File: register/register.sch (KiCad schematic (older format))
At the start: 38 parts, among them U1 74LS244, U2 74LS244, U3 74LS377, U4 74LS377

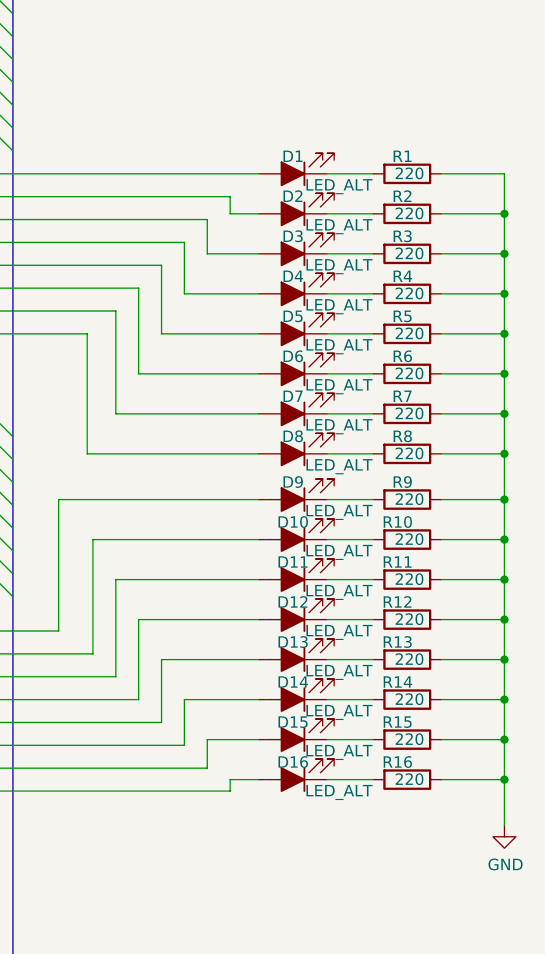
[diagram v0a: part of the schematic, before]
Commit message: route alu, upde register
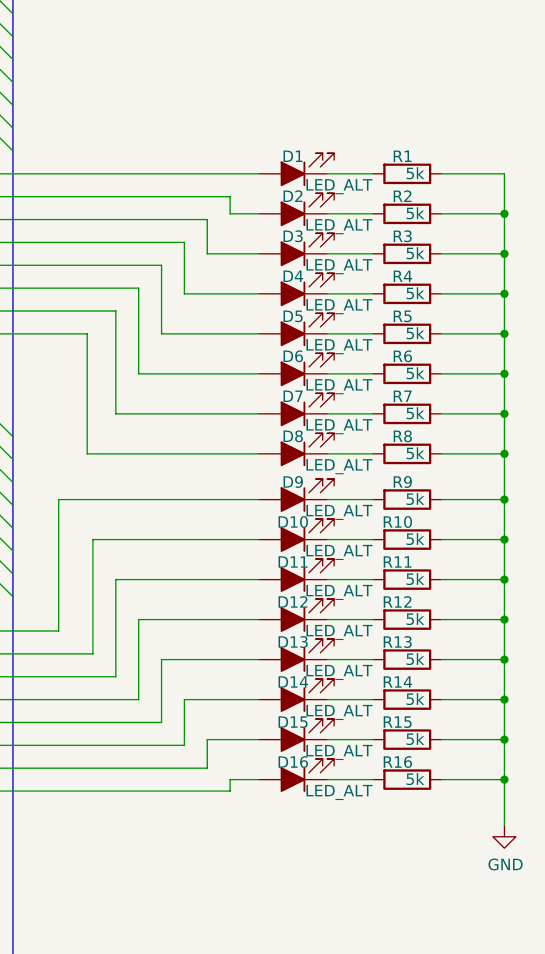
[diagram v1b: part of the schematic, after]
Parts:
- R1, R10, R11, R12, R13, R14, R15, R16, R2, R3, R4, R5, R6, R7, R8, R9: value 220 -> 5k
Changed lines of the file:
@@
 AR Path="/5EBAD929/5EC056B8" Ref="R2"  Part="1"
 F 0 "R2" V 10050 2475 50  0000 R CNN
-F 1 "220" V 10125 2525 50  0000 R CNN
+F 1 "5k" V 10125 2525 50  0000 R CNN
 F 2 "Resistor_THT:R_Axial_DIN0207_L6.3mm_D2.5mm_P7.62mm_Horizontal" V 10055 2450 50  0001 C CNN
 F 3 "~" H 10125 2450 50  0001 C CNN
@@
 AR Path="/5EBAD929/5EC056BE" Ref="R3"  Part="1"
 F 0 "R3" V 10050 2650 50  0000 R CNN
-F 1 "220" V 10125 2700 50  0000 R CNN
+F 1 "5k" V 10125 2700 50  0000 R CNN
 F 2 "Resistor_THT:R_Axial_DIN0207_L6.3mm_D2.5mm_P7.62mm_Horizontal" V 10055 2625 50  0001 C CNN
 F 3 "~" H 10125 2625 50  0001 C CNN
@@
 AR Path="/5EBAD929/5EC056C4" Ref="R4"  Part="1"
 F 0 "R4" V 10050 2825 50  0000 R CNN
-F 1 "220" V 10125 2875 50  0000 R CNN
+F 1 "5k" V 10125 2875 50  0000 R CNN
 F 2 "Resistor_THT:R_Axial_DIN0207_L6.3mm_D2.5mm_P7.62mm_Horizontal" V 10055 2800 50  0001 C CNN
 F 3 "~" H 10125 2800 50  0001 C CNN
@@
 AR Path="/5EBAD929/5EC056CA" Ref="R5"  Part="1"
 F 0 "R5" V 10050 3000 50  0000 R CNN
-F 1 "220" V 10125 3050 50  0000 R CNN
+F 1 "5k" V 10125 3050 50  0000 R CNN
 F 2 "Resistor_THT:R_Axial_DIN0207_L6.3mm_D2.5mm_P7.62mm_Horizontal" V 10055 2975 50  0001 C CNN
 F 3 "~" H 10125 2975 50  0001 C CNN
@@
 AR Path="/5EBAD929/5EC056D0" Ref="R6"  Part="1"
 F 0 "R6" V 10050 3175 50  0000 R CNN
-F 1 "220" V 10125 3225 50  0000 R CNN
+F 1 "5k" V 10125 3225 50  0000 R CNN
 F 2 "Resistor_THT:R_Axial_DIN0207_L6.3mm_D2.5mm_P7.62mm_Horizontal" V 10055 3150 50  0001 C CNN
 F 3 "~" H 10125 3150 50  0001 C CNN
@@
 AR Path="/5EBAD929/5EC056D6" Ref="R7"  Part="1"
 F 0 "R7" V 10050 3350 50  0000 R CNN
-F 1 "220" V 10125 3400 50  0000 R CNN
+F 1 "5k" V 10125 3400 50  0000 R CNN
 F 2 "Resistor_THT:R_Axial_DIN0207_L6.3mm_D2.5mm_P7.62mm_Horizontal" V 10055 3325 50  0001 C CNN
 F 3 "~" H 10125 3325 50  0001 C CNN
@@
 AR Path="/5EBAD929/5EC056DC" Ref="R8"  Part="1"
 F 0 "R8" V 10050 3525 50  0000 R CNN
-F 1 "220" V 10125 3575 50  0000 R CNN
+F 1 "5k" V 10125 3575 50  0000 R CNN
 F 2 "Resistor_THT:R_Axial_DIN0207_L6.3mm_D2.5mm_P7.62mm_Horizontal" V 10055 3500 50  0001 C CNN
 F 3 "~" H 10125 3500 50  0001 C CNN
@@
 AR Path="/5EBAD929/5EC056E2" Ref="R9"  Part="1"
 F 0 "R9" V 10050 3725 50  0000 R CNN
-F 1 "220" V 10125 3775 50  0000 R CNN
+F 1 "5k" V 10125 3775 50  0000 R CNN
 F 2 "Resistor_THT:R_Axial_DIN0207_L6.3mm_D2.5mm_P7.62mm_Horizontal" V 10055 3700 50  0001 C CNN
 F 3 "~" H 10125 3700 50  0001 C CNN
@@
 AR Path="/5EBAD929/5EC056E8" Ref="R10"  Part="1"
 F 0 "R10" V 10050 3900 50  0000 R CNN
-F 1 "220" V 10125 3950 50  0000 R CNN
+F 1 "5k" V 10125 3950 50  0000 R CNN
 F 2 "Resistor_THT:R_Axial_DIN0207_L6.3mm_D2.5mm_P7.62mm_Horizontal" V 10055 3875 50  0001 C CNN
 F 3 "~" H 10125 3875 50  0001 C CNN
@@
 AR Path="/5EBAD929/5EC056EE" Ref="R11"  Part="1"
 F 0 "R11" V 10050 4075 50  0000 R CNN
-F 1 "220" V 10125 4125 50  0000 R CNN
+F 1 "5k" V 10125 4125 50  0000 R CNN
 F 2 "Resistor_THT:R_Axial_DIN0207_L6.3mm_D2.5mm_P7.62mm_Horizontal" V 10055 4050 50  0001 C CNN
 F 3 "~" H 10125 4050 50  0001 C CNN
@@
 AR Path="/5EBAD929/5EC056F4" Ref="R12"  Part="1"
 F 0 "R12" V 10050 4250 50  0000 R CNN
-F 1 "220" V 10125 4300 50  0000 R CNN
+F 1 "5k" V 10125 4300 50  0000 R CNN
 F 2 "Resistor_THT:R_Axial_DIN0207_L6.3mm_D2.5mm_P7.62mm_Horizontal" V 10055 4225 50  0001 C CNN
 F 3 "~" H 10125 4225 50  0001 C CNN
@@
 AR Path="/5EBAD929/5EC056FA" Ref="R13"  Part="1"
 F 0 "R13" V 10050 4425 50  0000 R CNN
-F 1 "220" V 10125 4475 50  0000 R CNN
+F 1 "5k" V 10125 4475 50  0000 R CNN
 F 2 "Resistor_THT:R_Axial_DIN0207_L6.3mm_D2.5mm_P7.62mm_Horizontal" V 10055 4400 50  0001 C CNN
 F 3 "~" H 10125 4400 50  0001 C CNN
@@
 AR Path="/5EBAD929/5EC05700" Ref="R14"  Part="1"
 F 0 "R14" V 10050 4600 50  0000 R CNN
-F 1 "220" V 10125 4650 50  0000 R CNN
+F 1 "5k" V 10125 4650 50  0000 R CNN
 F 2 "Resistor_THT:R_Axial_DIN0207_L6.3mm_D2.5mm_P7.62mm_Horizontal" V 10055 4575 50  0001 C CNN
 F 3 "~" H 10125 4575 50  0001 C CNN
@@
 AR Path="/5EBAD929/5EC05706" Ref="R15"  Part="1"
 F 0 "R15" V 10050 4775 50  0000 R CNN
-F 1 "220" V 10125 4825 50  0000 R CNN
+F 1 "5k" V 10125 4825 50  0000 R CNN
 F 2 "Resistor_THT:R_Axial_DIN0207_L6.3mm_D2.5mm_P7.62mm_Horizontal" V 10055 4750 50  0001 C CNN
 F 3 "~" H 10125 4750 50  0001 C CNN
@@
 AR Path="/5EBAD929/5EC0570C" Ref="R16"  Part="1"
 F 0 "R16" V 10050 4950 50  0000 R CNN
-F 1 "220" V 10125 5000 50  0000 R CNN
+F 1 "5k" V 10125 5000 50  0000 R CNN
 F 2 "Resistor_THT:R_Axial_DIN0207_L6.3mm_D2.5mm_P7.62mm_Horizontal" V 10055 4925 50  0001 C CNN
 F 3 "~" H 10125 4925 50  0001 C CNN
@@
 AR Path="/5EBAD929/5EC0582D" Ref="R1"  Part="1"
 F 0 "R1" V 10050 2300 50  0000 R CNN
-F 1 "220" V 10125 2350 50  0000 R CNN
+F 1 "5k" V 10125 2350 50  0000 R CNN
 F 2 "Resistor_THT:R_Axial_DIN0207_L6.3mm_D2.5mm_P7.62mm_Horizontal" V 10055 2275 50  0001 C CNN
 F 3 "~" H 10125 2275 50  0001 C CNN
@@
 AR Path="/5EC05868" Ref="C?"  Part="1"
 AR Path="/5EBAD929/5EC05868" Ref="C1"  Part="1"
+AR Path="/5D3716A7/5EC05868" Ref="C1"  Part="1"
+AR Path="/5D35CB6B/5EC05868" Ref="C1"  Part="1"
 F 0 "C1" V 2177 6825 50  0000 C CNN
 F 1 "0.1µF" V 2086 6825 50  0000 C CNN
@@
 AR Path="/5EC0586E" Ref="#PWR?"  Part="1"
 AR Path="/5EBAD929/5EC0586E" Ref="#PWR01"  Part="1"
+AR Path="/5D3716A7/5EC0586E" Ref="#PWR01"  Part="1"
+AR Path="/5D35CB6B/5EC0586E" Ref="#PWR01"  Part="1"
 F 0 "#PWR01" H 1675 6675 50  0001 C CNN
 F 1 "VCC" V 1693 6952 50  0000 L CNN
@@
 AR Path="/5EC05875" Ref="#PWR?"  Part="1"
 AR Path="/5EBAD929/5EC05875" Ref="#PWR02"  Part="1"
+AR Path="/5D3716A7/5EC05875" Ref="#PWR02"  Part="1"
+AR Path="/5D35CB6B/5EC05875" Ref="#PWR02"  Part="1"
 F 0 "#PWR02" H 2175 6575 50  0001 C CNN
 F 1 "GND" V 2180 6697 50  0000 R CNN
@@
 AR Path="/5EC0587B" Ref="C?"  Part="1"
 AR Path="/5EBAD929/5EC0587B" Ref="C2"  Part="1"
+AR Path="/5D3716A7/5EC0587B" Ref="C2"  Part="1"
+AR Path="/5D35CB6B/5EC0587B" Ref="C2"  Part="1"
 F 0 "C2" V 2177 7300 50  0000 C CNN
 F 1 "0.1µF" V 2086 7300 50  0000 C CNN
@@
 Wire Wire Line
 	5150 1775 5150 4475
+Wire Wire Line
+	4850 1675 6150 1675
+Wire Wire Line
+	2100 1675 4850 1675
+Connection ~ 4850 1675
+Wire Wire Line
+	4850 1675 4850 2075
+Wire Wire Line
+	4450 2075 6150 2075
+Wire Wire Line
+	4550 1975 6150 1975
+Wire Wire Line
+	4650 1875 6150 1875
+Wire Wire Line
+	4750 1775 6150 1775
 Wire Bus Line
 	1700 6275 8400 6275
@@
 Wire Bus Line
 	8400 1475 8400 6275
-Wire Wire Line
-	4850 1675 6150 1675
-Wire Wire Line
-	2100 1675 4850 1675
-Connection ~ 4850 1675
-Wire Wire Line
-	4850 1675 4850 2075
-Wire Wire Line
-	4450 2075 6150 2075
-Wire Wire Line
-	4550 1975 6150 1975
-Wire Wire Line
-	4650 1875 6150 1875
-Wire Wire Line
-	4750 1775 6150 1775
 $EndSCHEMATC

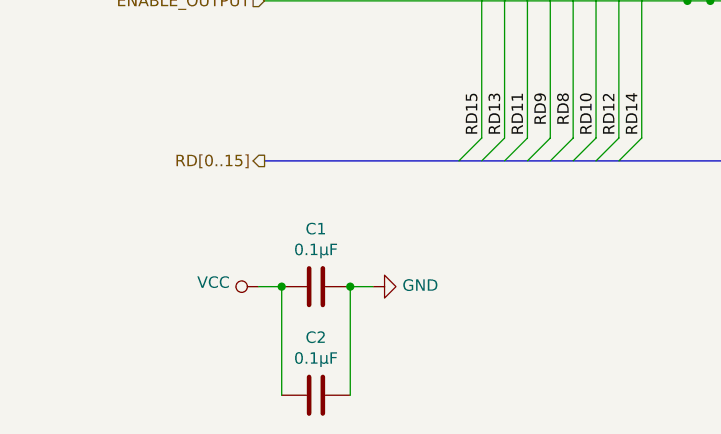
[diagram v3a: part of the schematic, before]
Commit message: connect cu and start creating material csv
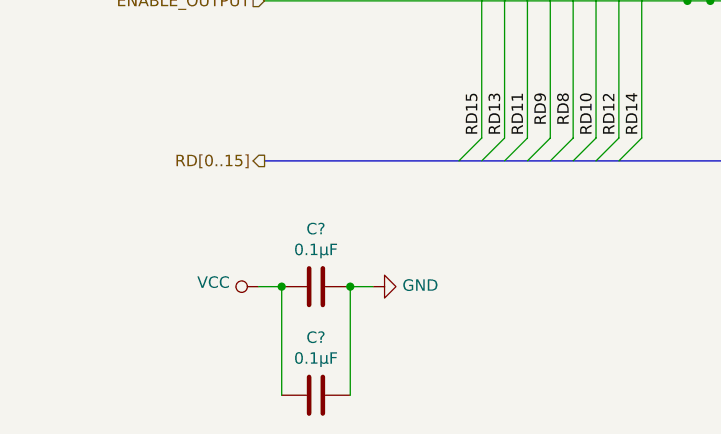
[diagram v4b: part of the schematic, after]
